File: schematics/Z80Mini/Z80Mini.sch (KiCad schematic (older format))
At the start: 22 parts, among them J1 Conn_02x20_Odd_Even, SW1 RESET, U1 Z80CPU, U2 TC55257CPI, U3 AT28C64B-15PU, U4 74LS32, U5 74HC14, X1 4MHz

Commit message: Added AY-3-8910 simple routine
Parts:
- U2: symbol Memory_RAM:TC55257CPI -> Z80Mini-rescue:TC55257CPI-Memory_RAM
- U3: symbol Memory_EEPROM:AT28C64B-15PU -> Z80Mini-rescue:AT28C64B-15PU-Memory_EEPROM
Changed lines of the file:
@@
 EESchema Schematic File Version 4
 LIBS:Z80Mini-cache
-EELAYER 29 0
+EELAYER 30 0
 EELAYER END
 $Descr A4 11693 8268
@@
 $EndComp
 $Comp
-L Memory_EEPROM:AT28C64B-15PU U3
+L Z80Mini-rescue:AT28C64B-15PU-Memory_EEPROM U3
 U 1 1 5D3D9F2C
 P 6450 2650
@@
 $EndComp
 $Comp
-L Memory_RAM:TC55257CPI U2
+L Z80Mini-rescue:TC55257CPI-Memory_RAM U2
 U 1 1 5D3DEAED
 P 4950 2500

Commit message: Latest modifications and update to v1.1 and first successifully VDP routines test.
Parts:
- removed C4: 100nF, Capacitor_THT:C_Disc_D7.0mm_W2.5mm_P5.00mm, symbol Device:C
- removed U3: AT28C64B-15PU, Package_DIP:DIP-28_W15.24mm_LongPads, symbol Z80Mini-rescue:AT28C64B-15PU-Memory_EEPROM
- removed U4: 74LS32, Package_DIP:DIP-14_W7.62mm_LongPads, symbol 74xx:74LS32
- removed unit 2 of U5
- removed unit 4 of U5
- added C13, C19: 100nF, Capacitor_THT:C_Disc_D7.0mm_W2.5mm_P5.00mm, symbol Device:C
- added C16: 10uF, Capacitor_THT:CP_Radial_D5.0mm_P2.50mm, symbol Device:CP
- added D4: LED, LED_THT:LED_D3.0mm, symbol Device:LED
- added Q1: BC337, Package_TO_SOT_THT:TO-92_Inline, symbol Transistor_BJT:BC337
- added R15: 1K, Resistor_THT:R_Axial_DIN0207_L6.3mm_D2.5mm_P7.62mm_Horizontal, symbol Device:R
- added R16: 330R, Resistor_THT:R_Axial_DIN0207_L6.3mm_D2.5mm_P7.62mm_Horizontal, symbol Device:R
- added R17: 10K, Resistor_THT:R_Axial_DIN0207_L6.3mm_D2.5mm_P7.62mm_Horizontal, symbol Device:R
- added U3: 28C256, Package_DIP:DIP-28_W15.24mm_LongPads, symbol Memory_EEPROM:28C256
- added U4: NE555, Package_DIP:DIP-8_W7.62mm_LongPads, symbol Timer:NE555
- added U6: 74LS139, Package_DIP:DIP-16_W7.62mm_LongPads, symbol 74xx_IEEE:74LS139
- R2: value 10K -> 100K
- R3: value 10 -> 47K
- U5: footprint (none) -> Package_DIP:DIP-14_W7.62mm_LongPads
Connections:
- net labels added: SND_SEL, VDP_SEL
- wire segments 240 -> 246
- no-connect marks 4 -> 5
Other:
- note added: "1.2"
- moved on the sheet: C5, U5G

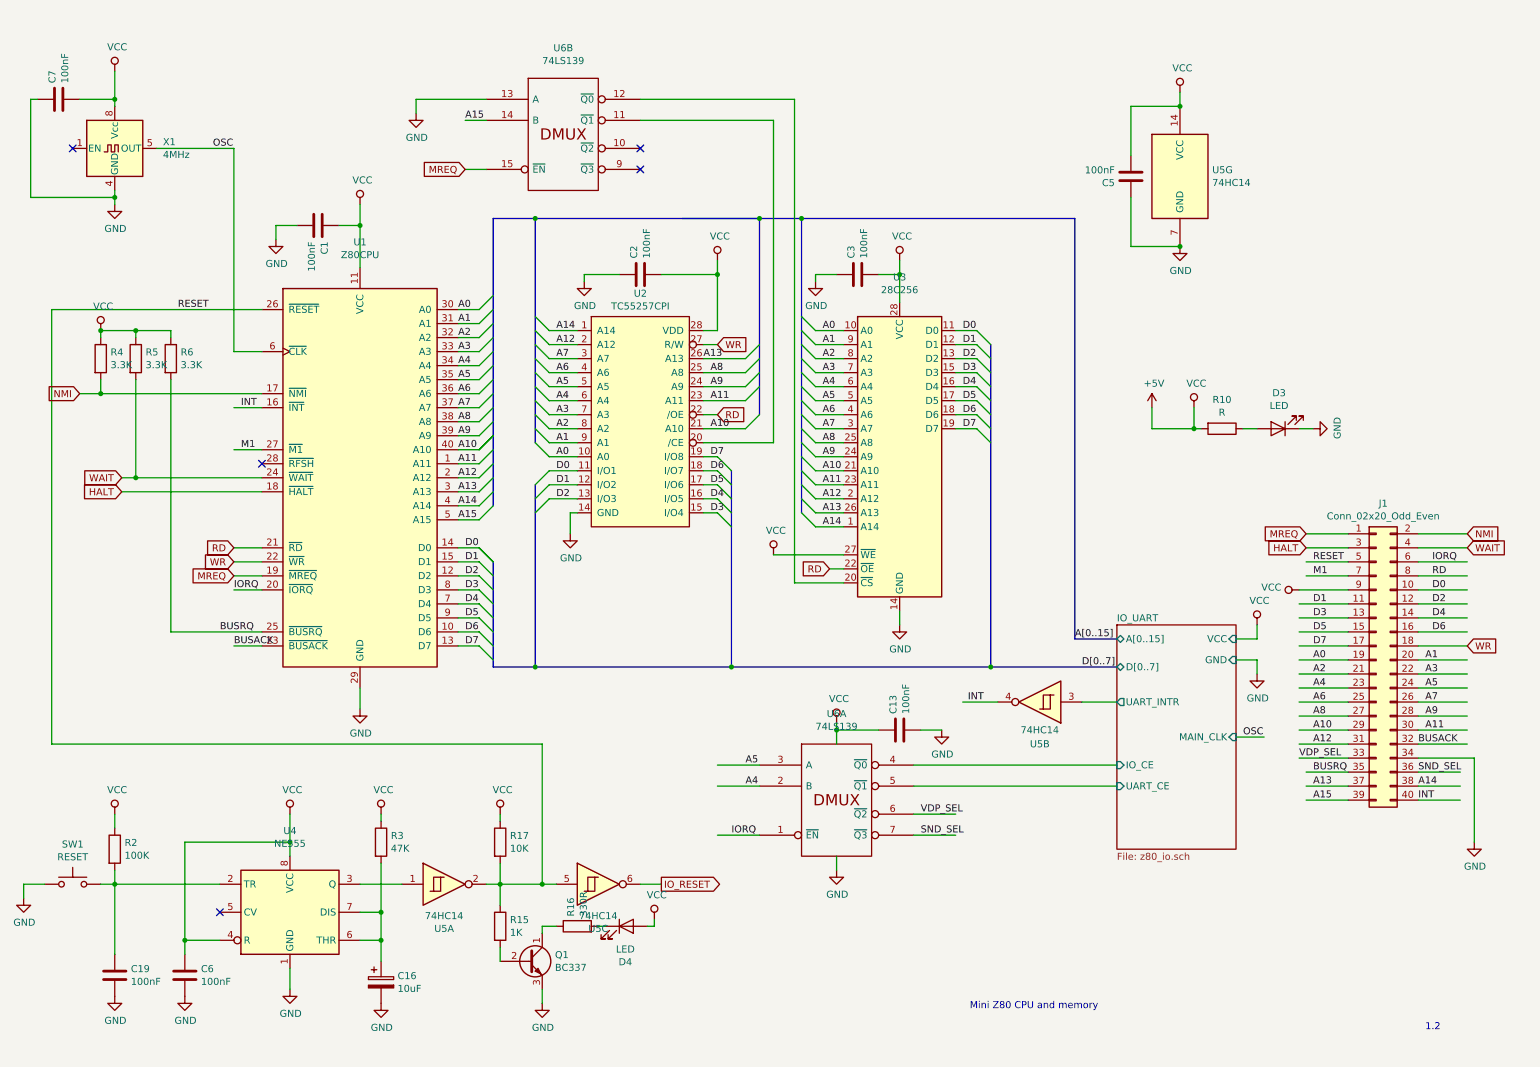
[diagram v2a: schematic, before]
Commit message: Added new code for core written in C with Z88DK
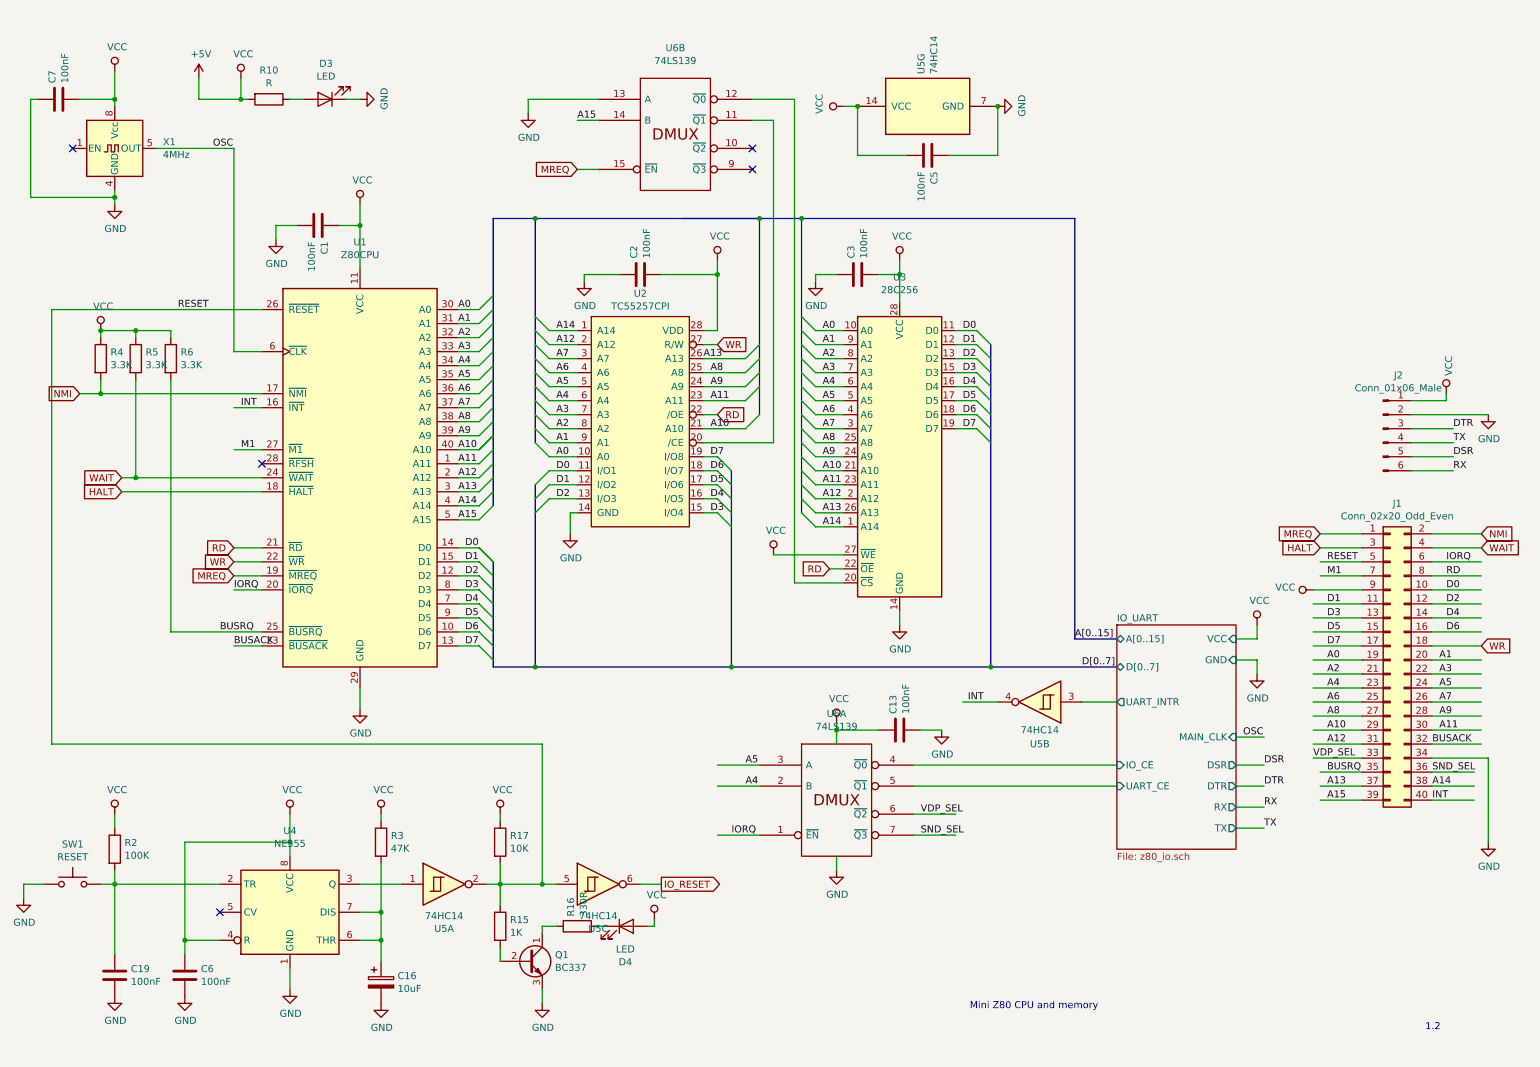
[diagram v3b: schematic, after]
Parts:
- added J2: Conn_01x06_Male, Connector_PinHeader_2.00mm:PinHeader_1x06_P2.00mm_Vertical, symbol Connector:Conn_01x06_Male
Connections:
- net labels added: DSR, DTR, RX, TX
- wire segments 246 -> 257
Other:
- moved on the sheet: C5, D3, J1, R10, U5G, U6B

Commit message: Testing C routines for VDP and keyboard. Generated backplane gerber files
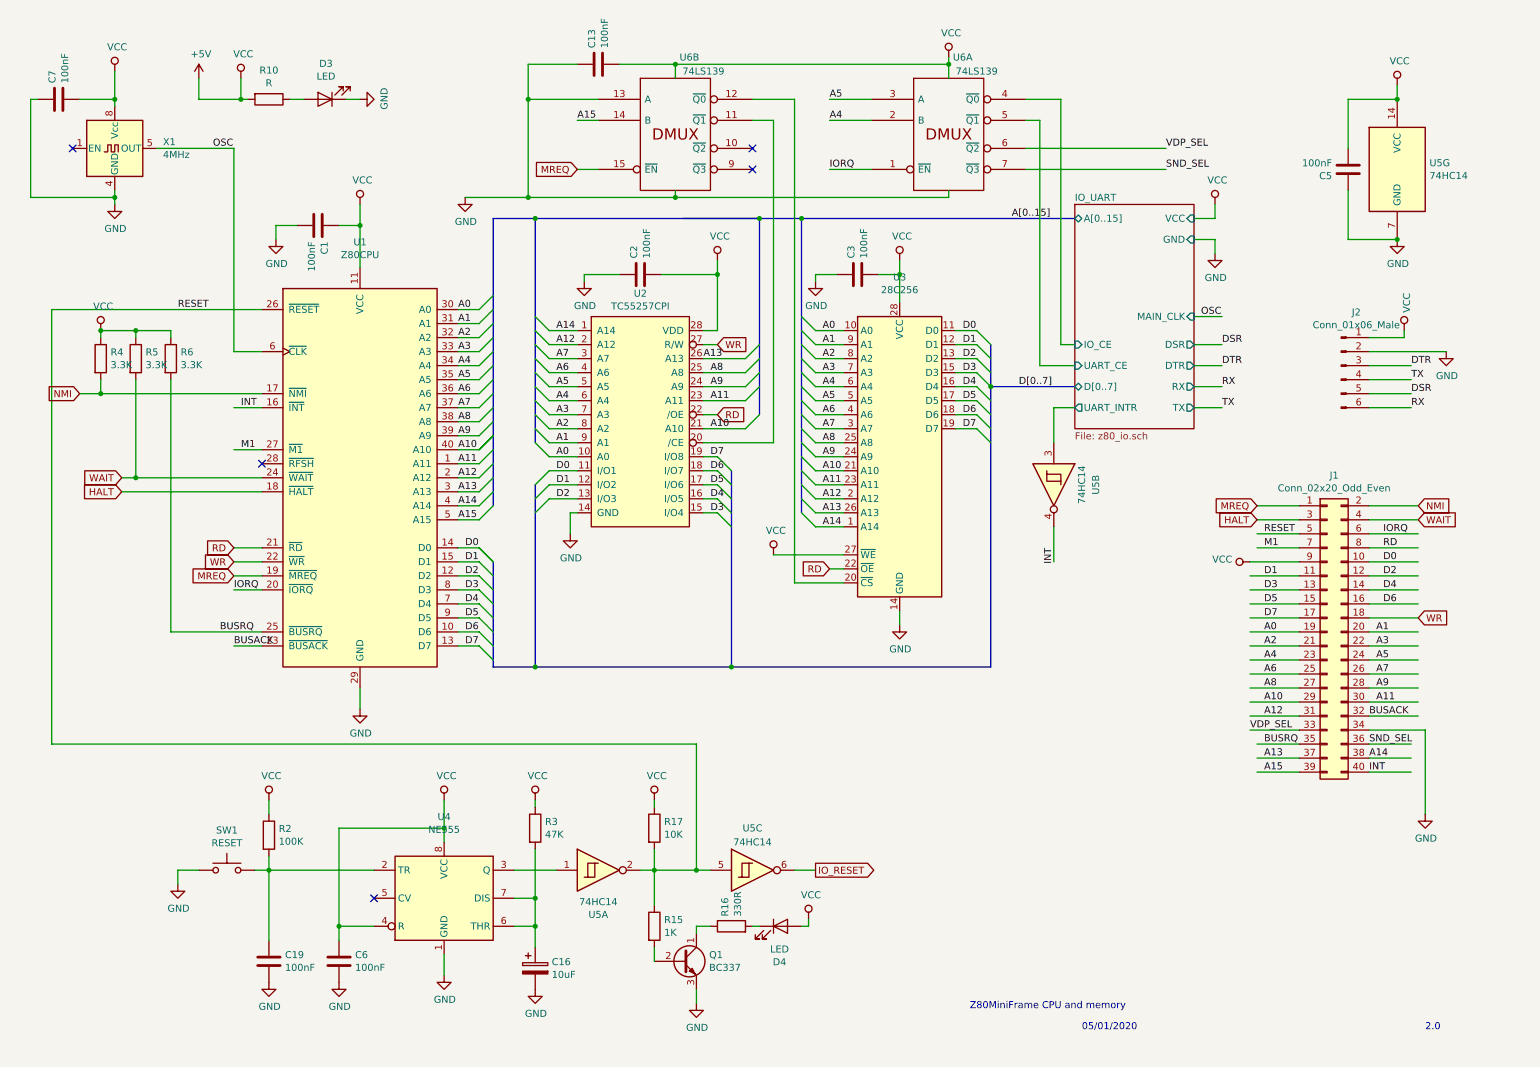
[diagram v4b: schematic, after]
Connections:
- wire segments 257 -> 269
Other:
- note added: "05/01/2020"
- note added: "2.0"
- note added: "Z80MiniFrame CPU and memory"
- note removed: "1.2"
- note removed: "Mini Z80 CPU and memory"
- moved on the sheet: C13, C16, C19, C5, C6, D4, J1, J2, Q1, R15, R16, R17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

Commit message: Latest changes on vdp routines and bas32k added new COLOR instruction
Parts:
- removed unit 3 of U5
- added unit 2 of U5
- J2: value Conn_01x06_Male -> TTL Serial; footprint Connector_PinHeader_2.00mm:PinHeader_1x06_P2.00mm_Vertical -> Connector_PinHeader_2.54mm:PinHeader_1x06_P2.54mm_Vertical
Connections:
- wire segments 269 -> 271
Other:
- note added: "08/06/2020"
- note removed: "05/01/2020"
- moved on the sheet: C16, C19, C6, D4, Q1, R15, R16, R17, R2, R3, SW1, U4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

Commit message: Latest changes
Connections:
- wire segments 271 -> 269
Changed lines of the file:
@@
 A12
-$Comp
-L 74xx:74HC14 U5
-U 7 1 5D7BCD08
-P 10400 1500
-F 0 "U5" H 10630 1546 50  0000 L CNN
-F 1 "74HC14" H 10630 1455 50  0000 L CNN
-F 2 "Package_DIP:DIP-14_W7.62mm_LongPads" H 10400 1500 50  0001 C CNN
-F 3 "http://www.ti.com/lit/gpn/sn74HC14" H 10400 1500 50  0001 C CNN
-	7    10400 1500
-	1    0    0    -1
-$EndComp
 $Comp
 L Device:C C5
@@
 Wire Wire Line
 	800  2500 2300 2500
-Text GLabel 4150 6150 1    50   Output ~ 0
-IO_RESET
 Wire Wire Line
 	1400 6500 1400 6400
@@
 Text Label 7650 1850 0    50   ~ 0
 A[0..15]
-$Comp
-L 74xx:74HC14 U5
-U 3 1 5DB892B7
-P 7950 3750
-F 0 "U5" H 7950 4050 50  0000 C CNN
-F 1 "74HC14" H 7950 3950 50  0000 C CNN
-F 2 "Package_DIP:DIP-14_W7.62mm_LongPads" H 7950 3750 50  0001 C CNN
-F 3 "http://www.ti.com/lit/gpn/sn74HC14" H 7950 3750 50  0001 C CNN
-	3    7950 3750
-	0    1    1    0
-$EndComp
 Text Label 7950 4200 3    50   ~ 0
 INT
@@
 Text Notes 8150 7650 0    50   ~ 0
 08/06/2020
-$Comp
-L 74xx:74HC14 U5
-U 1 1 5E307A0E
-P 3800 6500
-F 0 "U5" H 3800 6183 50  0000 C CNN
-F 1 "74HC14" H 3800 6274 50  0000 C CNN
-F 2 "Package_DIP:DIP-14_W7.62mm_LongPads" H 3800 6500 50  0001 C CNN
-F 3 "http://www.ti.com/lit/gpn/sn74HC14" H 3800 6500 50  0001 C CNN
-	1    3800 6500
-	1    0    0    -1
-$EndComp
 Wire Wire Line
 	4550 6350 4550 6500
@@
 Wire Wire Line
 	4550 6050 4550 6000
-Wire Wire Line
-	4150 6150 4150 6500
-Wire Wire Line
-	5500 5600 5500 6500
-$Comp
-L 74xx:74HC14 U5
-U 2 1 5EDF5D63
-P 5050 6500
-F 0 "U5" H 5050 6183 50  0000 C CNN
-F 1 "74HC14" H 5050 6274 50  0000 C CNN
-F 2 "Package_DIP:DIP-14_W7.62mm_LongPads" H 5050 6500 50  0001 C CNN
-F 3 "http://www.ti.com/lit/gpn/sn74HC14" H 5050 6500 50  0001 C CNN
-	2    5050 6500
-	1    0    0    -1
-$EndComp
-Wire Wire Line
-	800  5600 5500 5600
-Wire Wire Line
-	4100 6500 4150 6500
 Wire Wire Line
 	4650 7100 4650 7050
@@
 Wire Wire Line
 	4350 6500 4350 6900
-Wire Wire Line
-	5350 6500 5500 6500
 Connection ~ 4550 6500
 Wire Wire Line
 	4550 6500 4750 6500
-Connection ~ 4150 6500
 Wire Wire Line
 	3150 6500 3500 6500
@@
 	4350 6500 4550 6500
 Wire Wire Line
-	4150 6500 4350 6500
+	4100 6500 4350 6500
+Wire Wire Line
+	800  5600 4350 5600
+Wire Wire Line
+	4350 5600 4350 6500
+$Comp
+L 74xx:74HC14 U5
+U 7 1 5D7BCD08
+P 10400 1500
+F 0 "U5" H 10630 1546 50  0000 L CNN
+F 1 "74HC14" H 10630 1455 50  0000 L CNN
+F 2 "Package_DIP:DIP-14_W7.62mm_LongPads" H 10400 1500 50  0001 C CNN
+F 3 "http://www.ti.com/lit/gpn/sn74HC14" H 10400 1500 50  0001 C CNN
+	7    10400 1500
+	1    0    0    -1
+$EndComp
+$Comp
+L 74xx:74HC14 U5
+U 3 1 5DB892B7
+P 7950 3750
+F 0 "U5" H 7950 4050 50  0000 C CNN
+F 1 "74HC14" H 7950 3950 50  0000 C CNN
+F 2 "Package_DIP:DIP-14_W7.62mm_LongPads" H 7950 3750 50  0001 C CNN
+F 3 "http://www.ti.com/lit/gpn/sn74HC14" H 7950 3750 50  0001 C CNN
+	3    7950 3750
+	0    1    1    0
+$EndComp
+$Comp
+L 74xx:74HC14 U5
+U 1 1 5E307A0E
+P 3800 6500
+F 0 "U5" H 3800 6183 50  0000 C CNN
+F 1 "74HC14" H 3800 6274 50  0000 C CNN
+F 2 "Package_DIP:DIP-14_W7.62mm_LongPads" H 3800 6500 50  0001 C CNN
+F 3 "http://www.ti.com/lit/gpn/sn74HC14" H 3800 6500 50  0001 C CNN
+	1    3800 6500
+	1    0    0    -1
+$EndComp
+$Comp
+L 74xx:74HC14 U5
+U 2 1 5EDF5D63
+P 5050 6500
+F 0 "U5" H 5050 6183 50  0000 C CNN
+F 1 "74HC14" H 5050 6274 50  0000 C CNN
+F 2 "Package_DIP:DIP-14_W7.62mm_LongPads" H 5050 6500 50  0001 C CNN
+F 3 "http://www.ti.com/lit/gpn/sn74HC14" H 5050 6500 50  0001 C CNN
+	2    5050 6500
+	1    0    0    -1
+$EndComp
+Wire Bus Line
+	7500 2750 7500 3050
+Wire Bus Line
+	5850 1850 5850 3250
+Wire Bus Line
+	6150 1850 6150 3950
+Wire Bus Line
+	7500 3050 7500 5050
+Wire Bus Line
+	5650 3650 5650 5050
 Wire Bus Line
 	4250 3750 4250 5050
 Wire Bus Line
-	7500 2750 7500 3050
-Wire Bus Line
-	7500 3050 7500 5050
-Wire Bus Line
-	5650 3650 5650 5050
-Wire Bus Line
-	5850 1850 5850 3250
-Wire Bus Line
 	3950 4300 3950 5050
 Wire Bus Line
@@
 Wire Bus Line
 	3950 1850 3950 3900
-Wire Bus Line
-	6150 1850 6150 3950
+Text GLabel 5500 6500 2    50   Output ~ 0
+IO_RESET
+Wire Wire Line
+	5350 6500 5500 6500
 $EndSCHEMATC
